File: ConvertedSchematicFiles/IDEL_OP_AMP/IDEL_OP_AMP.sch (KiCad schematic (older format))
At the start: 13 parts

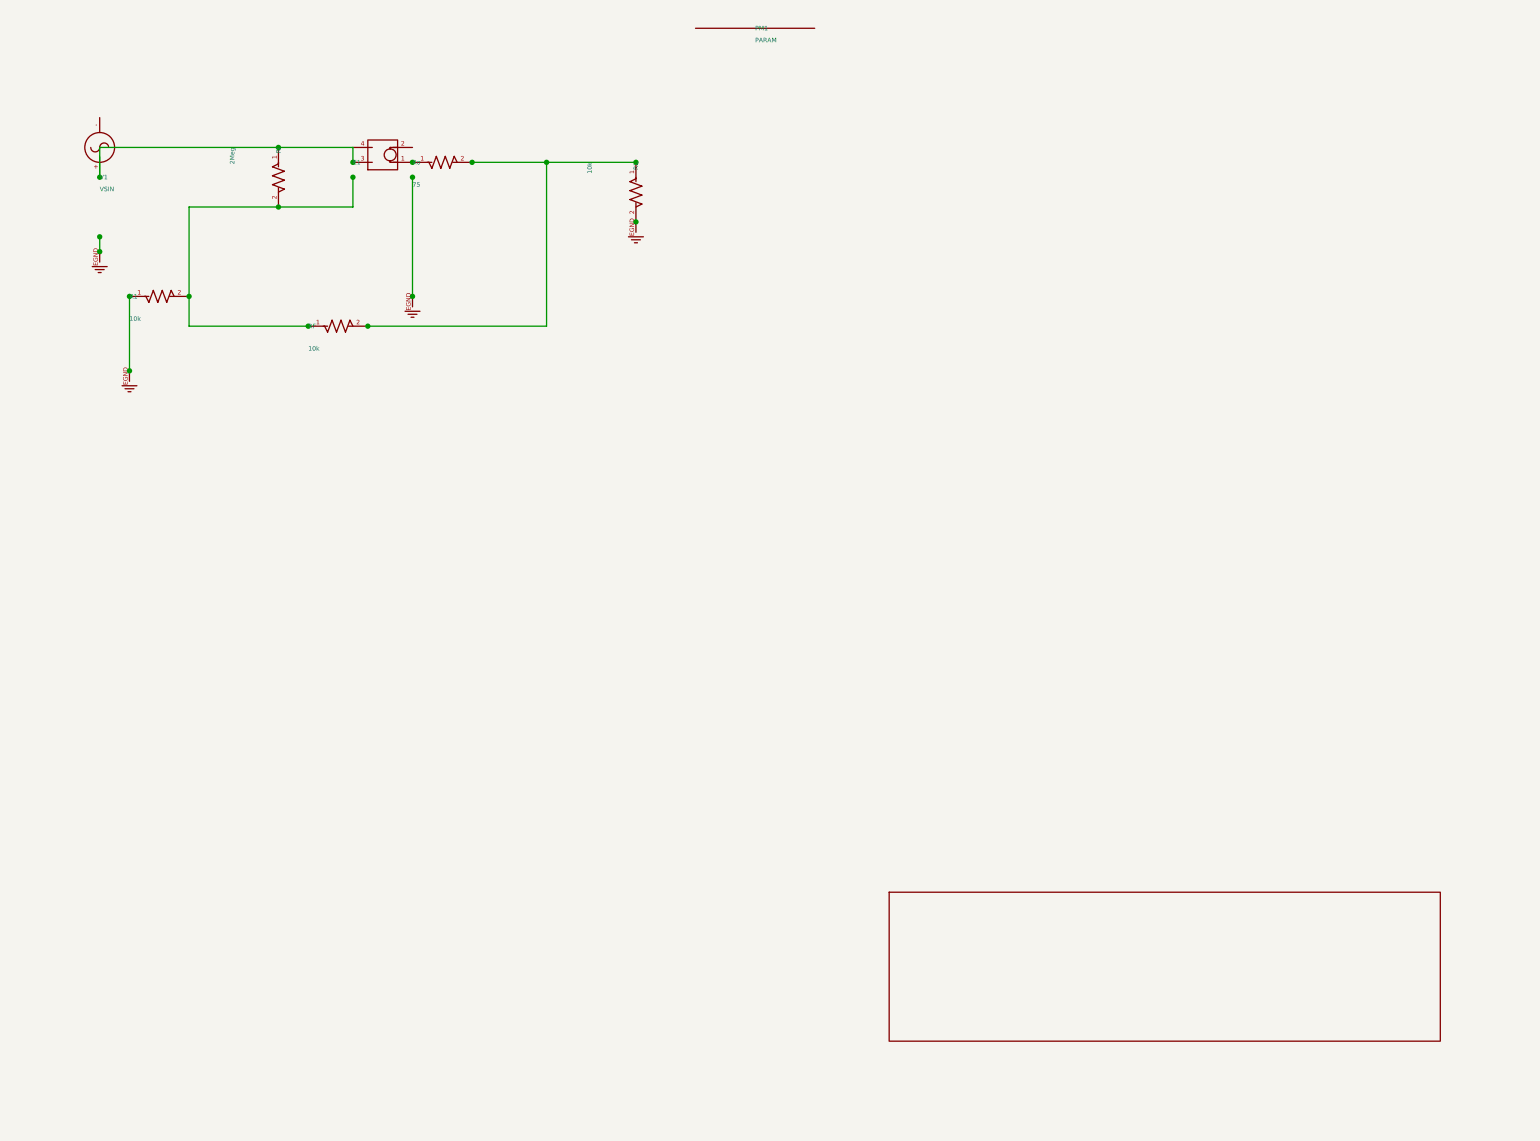
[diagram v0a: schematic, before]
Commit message: Excluded some components. These no longer appear after conversion. When calling shell commands, filenames are in "quotes"
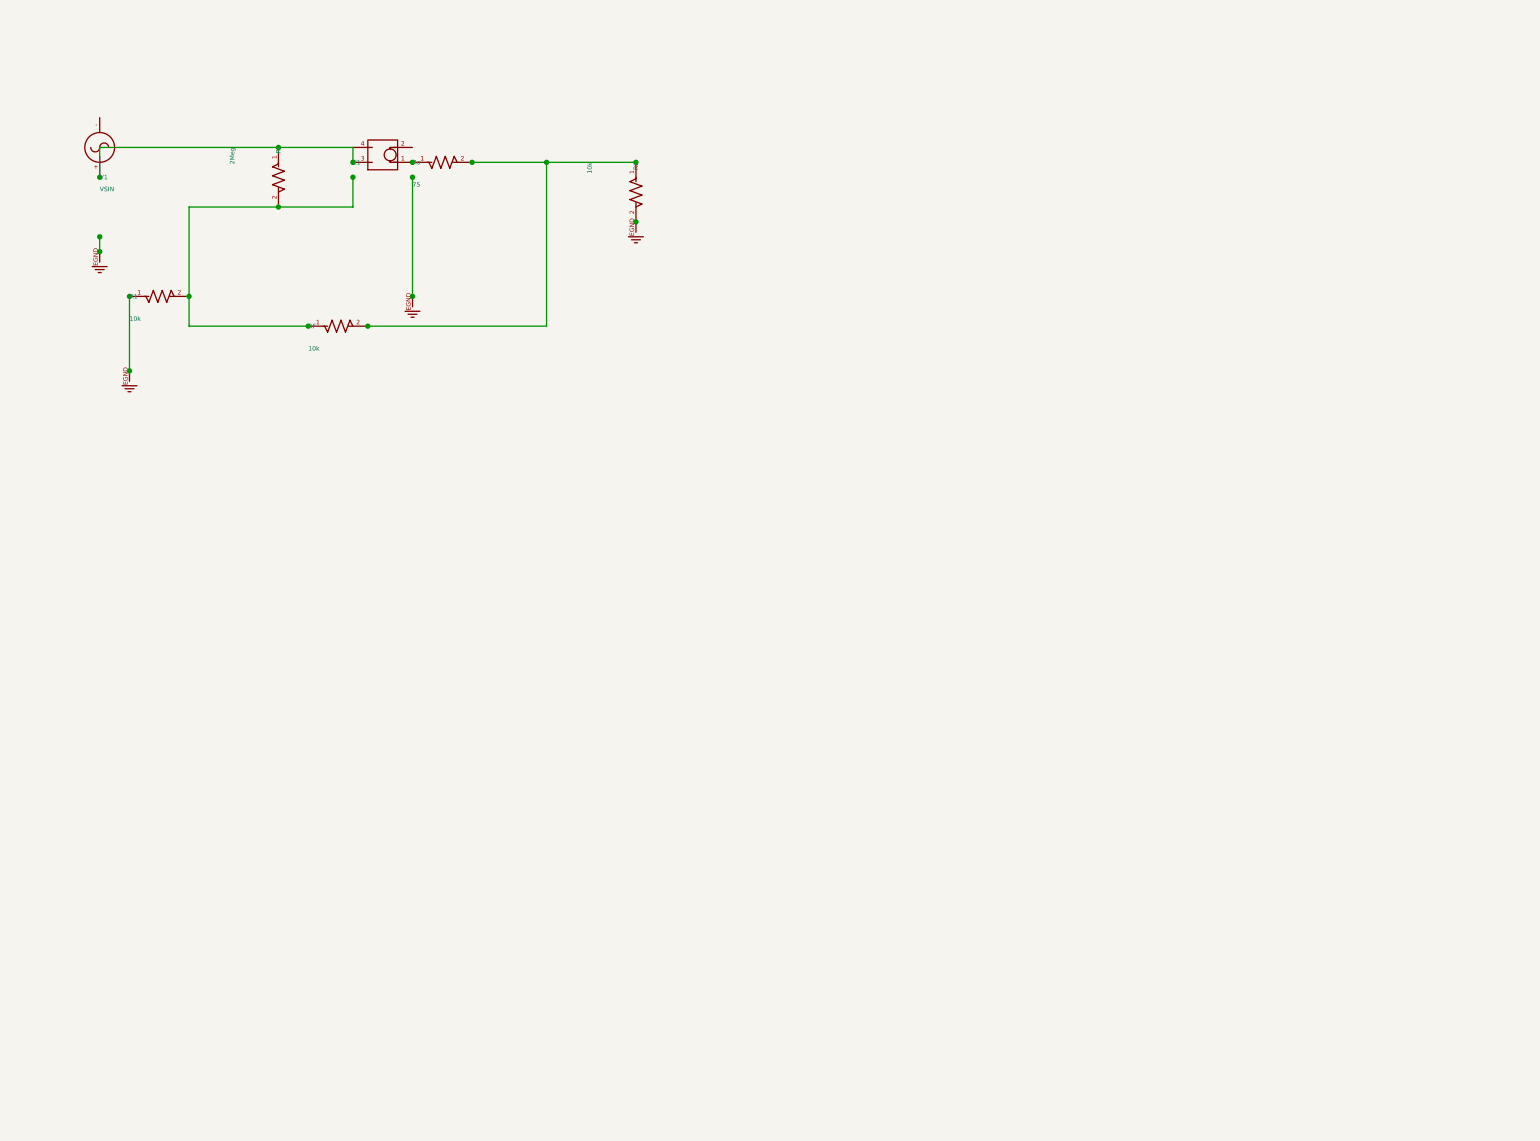
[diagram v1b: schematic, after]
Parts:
- removed PM1: PARAM, symbol PARAM_PSPICE
- removed titleblk: titleblk, symbol TITLEBLK_PSPICE
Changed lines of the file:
@@
-	1    0    0    1
-$EndComp
-$Comp
-L PARAM_PSPICE PM1
-U 1 1 10490027
-P 5100 400
-F 0 "PM1" H 5100 400 30  0000 L CNN
-F 1 "PARAM" H 5100 480 30  0000 L CNN
-	1    5100 400
-	1    0    0    1
-$EndComp
-$Comp
-L TITLEBLK_PSPICE titleblk
-U 1 1 73368690
-P 9700 7200
-F 0 "titleblk" H 19400 14400 30  0001 L CNN
-F 1 "titleblk" H 19400 14480 30  0001 L CNN
-	1    9700 7200
 	1    0    0    1
 $EndComp

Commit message: Ports issue fixed. Now annotation for ports is #PWR? function added "itos"
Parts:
- removed EGND (x4): EGND, symbol EGND_PSPICE
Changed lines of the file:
@@
 $EndDescr
 $Comp
-L EGND_PSPICE EGND
+L EGND_PSPICE #PWR1
 U 1 1 14289383
 P 2800 2200
-F 0 "EGND" H 5600 4400 30  0001 L CNN
+F 0 "#PWR1" H 5600 4400 30  0001 L CNN
 F 1 "EGND" H 5600 4480 30  0001 L CNN
 	1    2800 2200
@@
 $EndComp
 $Comp
-L EGND_PSPICE EGND
+L EGND_PSPICE #PWR2
 U 1 1 46930886
 P 900 2700
-F 0 "EGND" H 1800 5400 30  0001 L CNN
+F 0 "#PWR2" H 1800 5400 30  0001 L CNN
 F 1 "EGND" H 1800 5480 30  0001 L CNN
 	1    900 2700
@@
 $EndComp
 $Comp
-L EGND_PSPICE EGND
+L EGND_PSPICE #PWR3
 U 1 1 71692777
 P 700 1900
-F 0 "EGND" H 1400 3800 30  0001 L CNN
+F 0 "#PWR3" H 1400 3800 30  0001 L CNN
 F 1 "EGND" H 1400 3880 30  0001 L CNN
 	1    700 1900
@@
 $EndComp
 $Comp
-L EGND_PSPICE EGND
+L EGND_PSPICE #PWR4
 U 1 1 14636915
 P 4300 1700
-F 0 "EGND" H 8600 3400 30  0001 L CNN
+F 0 "#PWR4" H 8600 3400 30  0001 L CNN
 F 1 "EGND" H 8600 3480 30  0001 L CNN
 	1    4300 1700

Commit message: Added LICENSE.txt
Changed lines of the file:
@@
 $EndDescr
 $Comp
-L EGND_PSPICE #PWR1
+L GND #PWR1
 U 1 1 14289383
 P 2800 2200
@@
 $EndComp
 $Comp
-L EGND_PSPICE #PWR2
+L GND #PWR2
 U 1 1 46930886
 P 900 2700
@@
 $EndComp
 $Comp
-L EGND_PSPICE #PWR3
+L GND #PWR3
 U 1 1 71692777
 P 700 1900
@@
 $EndComp
 $Comp
-L EGND_PSPICE #PWR4
+L GND #PWR4
 U 1 1 14636915
 P 4300 1700

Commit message: Orientation fix. Library components are now inverted, with +ve y axis going up. In Schematic files, +ve y axis is downwards. This is how the KiCad libraries are. As a result of the above fixed, the converted GND is now oriented correctly.
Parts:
- V1: value VSIN -> SINE
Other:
- moved on the sheet: E1, V1
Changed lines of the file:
@@
 F 1 "EGND" H 5600 4480 30  0001 L CNN
 	1    2800 2200
-	1    0    0    1
+	1    0    0    -1
 $EndComp
 $Comp
@@
 F 1 "EGND" H 1800 5480 30  0001 L CNN
 	1    900 2700
-	1    0    0    1
+	1    0    0    -1
 $EndComp
 $Comp
@@
 F 1 "EGND" H 1400 3880 30  0001 L CNN
 	1    700 1900
-	1    0    0    1
+	1    0    0    -1
 $EndComp
 $Comp
@@
 F 1 "EGND" H 8600 3480 30  0001 L CNN
 	1    4300 1700
-	1    0    0    1
+	1    0    0    -1
 $EndComp
 $Comp
@@
 F 1 "2Meg" H 1900 1510 30  0000 L CNN
 	1    1900 1200
-	0    -1    1    0
+	0    1    1    0
 $EndComp
 $Comp
@@
 P 700 1400
 F 0 "V1" H 700 1400 30  0000 L CNN
-F 1 "VSIN" H 700 1480 30  0000 L CNN
+F 1 "SINE" H 700 1480 30  0000 L CNN
 	1    700 1400
-	1    0    0    1
+	1    0    0    -1
 $EndComp
 $Comp
@@
 F 1 "10k" H 4300 1610 30  0000 L CNN
 	1    4300 1300
-	0    -1    1    0
+	0    1    1    0
 $EndComp
 $Comp
@@
 F 1 "10k" H 2100 2550 30  0000 L CNN
 	1    2100 2400
-	1    0    0    1
+	1    0    0    -1
 $EndComp
 $Comp
@@
 F 1 "-200000" H 2400 1300 30  0001 L CNN
 	1    2400 1300
-	1    0    0    1
+	1    0    0    -1
 $EndComp
 $Comp
@@
 F 1 "10k" H 900 2350 30  0000 L CNN
 	1    900 2200
-	1    0    0    1
+	1    0    0    -1
 $EndComp
 $Comp
@@
 F 1 "75" H 2800 1450 30  0000 L CNN
 	1    2800 1300
-	1    0    0    1
+	1    0    0    -1
 $EndComp
 Wire Wire Line

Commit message: Removed the use of exec, wrote basename function, made integration with eSim easier.
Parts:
- added PM1: PARAM, symbol PARAM_PSPICE
- added titleblk: titleblk, symbol titleblk_PSPICE
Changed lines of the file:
@@
-EESchema Schematic File Version 2  date Monday 21 June 1999 07:18:17 PM IST
+EESchema Schematic File Version 2  date
 LIBS:power
 LIBS:device
@@
 LIBS:contrib
 LIBS:valves
-LIBS:ConvertedSchematicFiles/IDEL_OP_AMP-cache
 EELAYER 25  0
 EELAYER END
@@
 Sheet 1 1
 Title ""
-Date "21 Jun 1999"
+Date ""
 Rev ""
 Comp ""
@@
 	1    0    0    -1
 $EndComp
+$Comp
+L PARAM_PSPICE PM1
+U 1 1 10490027
+P 5100 400
+F 0 "PM1" H 5100 400 30  0000 L CNN
+F 1 "PARAM" H 5100 480 30  0000 L CNN
+	1    5100 400
+	1    0    0    -1
+$EndComp
+$Comp
+L titleblk_PSPICE titleblk
+U 1 1 73368690
+P 9700 7200
+F 0 "titleblk" H 19400 14400 30  0001 L CNN
+F 1 "titleblk" H 19400 14480 30  0001 L CNN
+	1    9700 7200
+	1    0    0    -1
+$EndComp
